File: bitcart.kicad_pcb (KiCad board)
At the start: 4 copper layers, 160 x 90 mm, 151 parts, among them J1 Conn_01x03, J10 690-019-298-412, J11 USB_OTG, J12 10018783-11200TLF, J13 690-008-221-904, J14 Conn_02x05_Odd_Even, J15 Conn_01x22_Female, J16 Conn_01x22_Female, J17 Molex 470531000, J19 Barrel_Jack, J2 Conn_02x07_Odd_Even, J20 AMP171826-4, J22 690-019-298-412, J3 Conn_01x03, J4 Conn_01x22_Female, J5 Conn_01x22_Female, J6 THD-02-R, J7 Micro_SD_Card_Det, J8 THD-20-R, J9 THD-02-R, Q1 DMP3013SFV-7, U1 TPD4EUSB30, U11 EMC2301-1-ACZL-TR, U12 RT9742SNGV, U13 FSUSB42MUX, U14 74LVC1G07SE-7, U15 AP64501SP-13, U16 AP64501SP-13, U18 RT9742GGJ5, U2 TPD4EUSB30, U3 MagJack-A70-112-331N126, U4 TPD4EUSB30, U5 74LVC1G07SE-7, U6 USB2514B-I/M2, U7 AP22653W6, U8 PCF85063AT/AAZ, U9 74LVC1G07SE-7, Y1 24MHz, Y2 X32K768S301

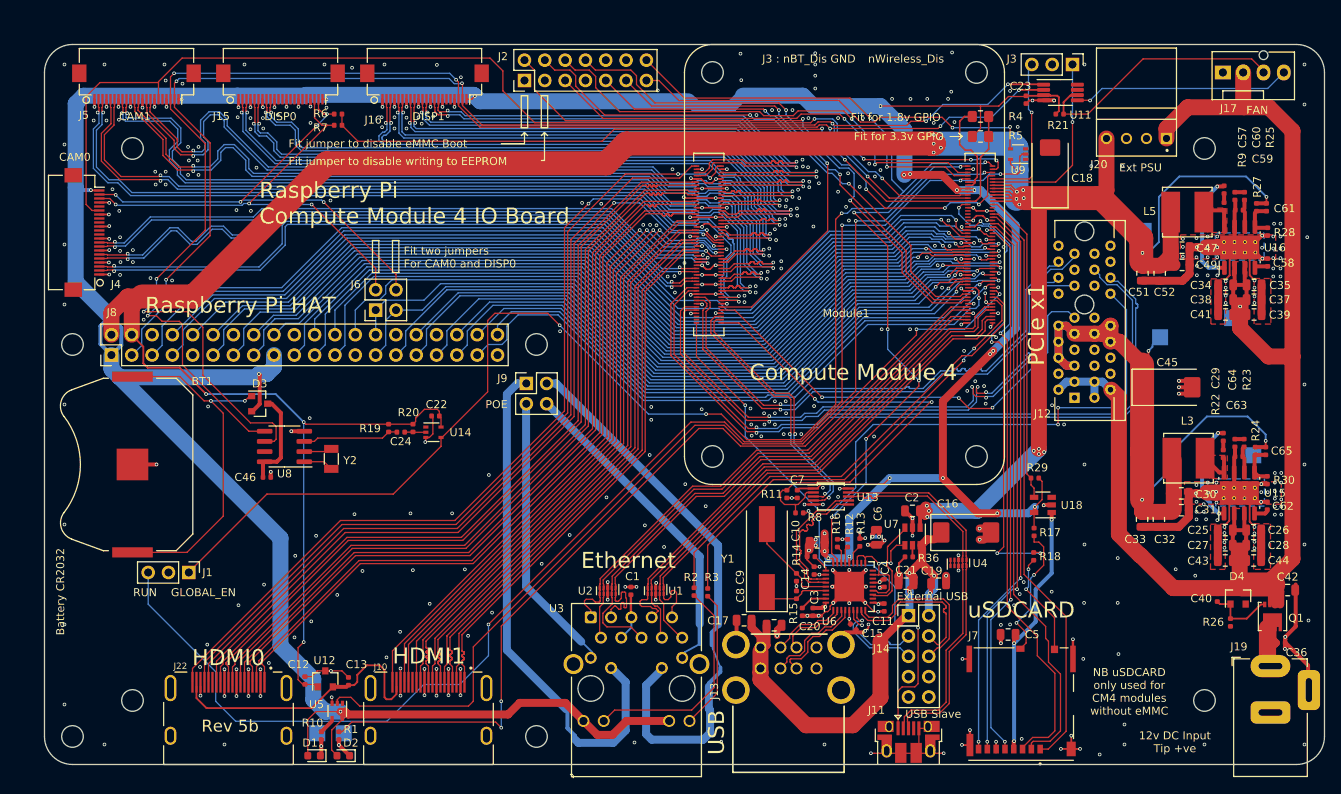
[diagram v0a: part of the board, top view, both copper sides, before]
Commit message: removed many unused parts
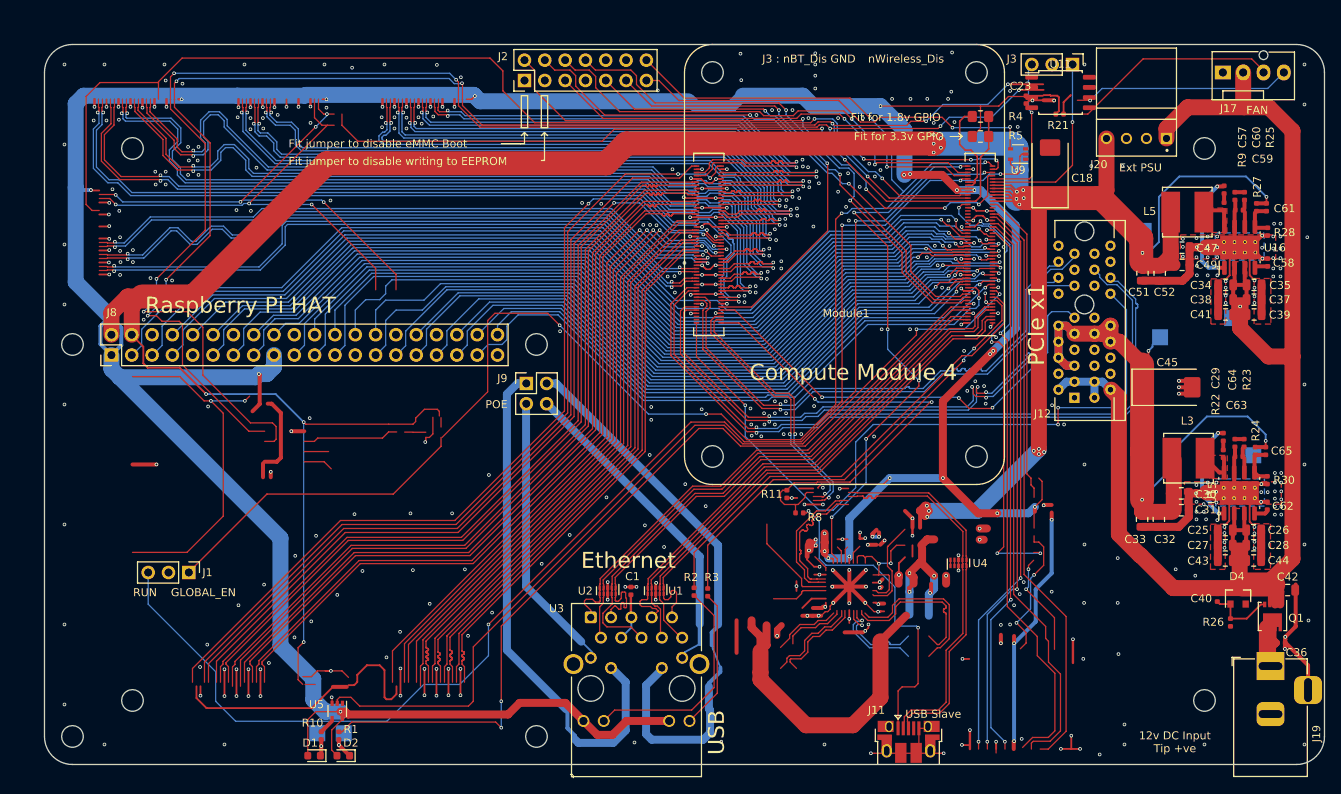
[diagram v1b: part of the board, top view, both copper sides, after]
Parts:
- removed BT1: Battery_Cell, Battery:BatteryHolder_Keystone_3034_1x20mm
- removed C10, C17, C19, C2, C20, C21, C5, C6: 10u, Capacitor_SMD:C_0805_2012Metric
- removed C11, C12, C13, C14, C15, C22, C24, C3, C4, C46, C7: 100n, Capacitor_SMD:C_0402_1005Metric
- removed C16: 100uF, Capacitor_Tantalum_SMD:CP_EIA-7343-31_Kemet-D
- removed C8, C9: 27pF, Capacitor_SMD:C_0402_1005Metric
- removed D3: BAT54C-7-F, Package_TO_SOT_SMD:SOT-23
- removed J10, J22: 690-019-298-412, CM4IO:EDAC 690-019-298-412
- removed J13: 690-008-221-904, CM4IO:MOLEX_USB_67298-4090
- removed J14: Conn_02x05_Odd_Even, Connector_PinHeader_2.54mm:PinHeader_2x05_P2.54mm_Vertical
- removed J15, J16, J4, J5: Conn_01x22_Female, CM4IO:Hirose_FH12-22S-0.5SH_1x22-1MP_P0.50mm_Horizontal
- removed J6: THD-02-R, Connector_PinHeader_2.54mm:PinHeader_2x02_P2.54mm_Vertical
- removed J7: Micro_SD_Card_Det, CM4IO:SDCARD_MOLEX_503398-1892
- removed R12, R13, R14, R16: 36K 1%, Resistor_SMD:R_0402_1005Metric
- removed R15, R29: 12K 1%, Resistor_SMD:R_0402_1005Metric
- removed R17, R18: nf, Resistor_SMD:R_0402_1005Metric
- removed R19, R20: 510K 1%, Resistor_SMD:R_0402_1005Metric
- removed R36: 15K 1%, Resistor_SMD:R_0402_1005Metric
- removed R6, R7: 2.2K 1%, Resistor_SMD:R_0402_1005Metric
- removed U12: RT9742SNGV, Package_TO_SOT_SMD:SOT-23
- removed U13: FSUSB42MUX, Package_SO:MSOP-10_3x3mm_P0.5mm
- removed U14: 74LVC1G07SE-7, Package_TO_SOT_SMD:SOT-353_SC-70-5
- removed U18: RT9742GGJ5, Package_TO_SOT_SMD:SOT-23-5
- removed U6: USB2514B-I/M2, Package_DFN_QFN:QFN-36-1EP_6x6mm_P0.5mm_EP3.7x3.7mm
- removed U7: AP22653W6, Package_TO_SOT_SMD:SOT-23-6
- removed U8: PCF85063AT/AAZ, Package_SO:SOIC-8_3.9x4.9mm_P1.27mm
- removed Y1: 24MHz, Crystal:Crystal_SMD_HC49-SD
- removed Y2: X32K768S301, Crystal:Crystal_SMD_3215-2Pin_3.2x1.5mm
- J19: footprint CM4IO:BarrelJack_Horizontal -> Connector_BarrelJack:BarrelJack_Horizontal
- U11: footprint Package_SO:MSOP-8_3x3mm_P0.65mm -> Package_SO:SOIC-8_5.23x5.23mm_P1.27mm
- U15: footprint CM4IO:SOIC-8-1EP_3.9x4.9mm_P1.27mm_EP2.95x4.9mm_Mask2.71x3.4mm_ThermalVias -> Package_SO:SOIC-8-1EP_3.9x4.9mm_P1.27mm_EP2.95x4.9mm_Mask2.71x3.4mm_ThermalVias
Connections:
- Module1 pad 115: /CM4_HighSpeed/CAM1_D0_N -> unconnected-(Module1-Pad115)
- Module1 pad 117: /CM4_HighSpeed/CAM1_D0_P -> unconnected-(Module1-Pad117)
- Module1 pad 121: /CM4_HighSpeed/CAM1_D1_N -> unconnected-(Module1-Pad121)
- Module1 pad 123: /CM4_HighSpeed/CAM1_D1_P -> unconnected-(Module1-Pad123)
- Module1 pad 127: /CM4_HighSpeed/CAM1_C_N -> unconnected-(Module1-Pad127)
- Module1 pad 128: /CM4_HighSpeed/CAM0_D0_N -> unconnected-(Module1-Pad128)
- Module1 pad 129: /CM4_HighSpeed/CAM1_C_P -> unconnected-(Module1-Pad129)
- Module1 pad 130: /CM4_HighSpeed/CAM0_D0_P -> unconnected-(Module1-Pad130)
- Module1 pad 133: /CM4_HighSpeed/CAM1_D2_N -> unconnected-(Module1-Pad133)
- Module1 pad 134: /CM4_HighSpeed/CAM0_D1_N -> unconnected-(Module1-Pad134)
- Module1 pad 135: /CM4_HighSpeed/CAM1_D2_P -> unconnected-(Module1-Pad135)
- Module1 pad 136: /CM4_HighSpeed/CAM0_D1_P -> unconnected-(Module1-Pad136)
- Module1 pad 139: /CM4_HighSpeed/CAM1_D3_N -> unconnected-(Module1-Pad139)
- Module1 pad 140: /CM4_HighSpeed/CAM0_C_N -> unconnected-(Module1-Pad140)
- Module1 pad 141: /CM4_HighSpeed/CAM1_D3_P -> unconnected-(Module1-Pad141)
- Module1 pad 142: /CM4_HighSpeed/CAM0_C_P -> unconnected-(Module1-Pad142)
- Module1 pad 143: /CM4_HighSpeed/HDMI1_HOTPLUG -> unconnected-(Module1-Pad143)
- Module1 pad 145: /CM4_HighSpeed/HDMI1_SDA -> unconnected-(Module1-Pad145)
- Module1 pad 146: /CM4_HighSpeed/HDMI1_D2_P -> unconnected-(Module1-Pad146)
- Module1 pad 147: /CM4_HighSpeed/HDMI1_SCL -> unconnected-(Module1-Pad147)
- Module1 pad 148: /CM4_HighSpeed/HDMI1_D2_N -> unconnected-(Module1-Pad148)
- Module1 pad 149: /CM4_HighSpeed/HDMI1_CEC -> unconnected-(Module1-Pad149)
- Module1 pad 151: /CM4_HighSpeed/HDMI0_CEC -> unconnected-(Module1-Pad151)
- Module1 pad 152: /CM4_HighSpeed/HDMI1_D1_P -> unconnected-(Module1-Pad152)
- Module1 pad 153: /CM4_HighSpeed/HDMI0_HOTPLUG -> unconnected-(Module1-Pad153)
- Module1 pad 154: /CM4_HighSpeed/HDMI1_D1_N -> unconnected-(Module1-Pad154)
- Module1 pad 157: /CM4_HighSpeed/DSI0_D0_N -> unconnected-(Module1-Pad157)
- Module1 pad 158: /CM4_HighSpeed/HDMI1_D0_P -> unconnected-(Module1-Pad158)
- Module1 pad 159: /CM4_HighSpeed/DSI0_D0_P -> unconnected-(Module1-Pad159)
- Module1 pad 160: /CM4_HighSpeed/HDMI1_D0_N -> unconnected-(Module1-Pad160)
- Module1 pad 163: /CM4_HighSpeed/DSI0_D1_N -> unconnected-(Module1-Pad163)
- Module1 pad 164: /CM4_HighSpeed/HDMI1_CK_P -> unconnected-(Module1-Pad164)
- Module1 pad 165: /CM4_HighSpeed/DSI0_D1_P -> unconnected-(Module1-Pad165)
- Module1 pad 166: /CM4_HighSpeed/HDMI1_CK_N -> unconnected-(Module1-Pad166)
- Module1 pad 169: /CM4_HighSpeed/DSI0_C_N -> unconnected-(Module1-Pad169)
- Module1 pad 170: /CM4_HighSpeed/HDMI0_D2_P -> unconnected-(Module1-Pad170)
- Module1 pad 171: /CM4_HighSpeed/DSI0_C_P -> unconnected-(Module1-Pad171)
- Module1 pad 172: /CM4_HighSpeed/HDMI0_D2_N -> unconnected-(Module1-Pad172)
- Module1 pad 175: /CM4_HighSpeed/DSI1_D0_N -> unconnected-(Module1-Pad175)
- Module1 pad 176: /CM4_HighSpeed/HDMI0_D1_P -> unconnected-(Module1-Pad176)
- Module1 pad 177: /CM4_HighSpeed/DSI1_D0_P -> unconnected-(Module1-Pad177)
- Module1 pad 178: /CM4_HighSpeed/HDMI0_D1_N -> unconnected-(Module1-Pad178)
- Module1 pad 181: /CM4_HighSpeed/DSI1_D1_N -> unconnected-(Module1-Pad181)
- Module1 pad 182: /CM4_HighSpeed/HDMI0_D0_P -> unconnected-(Module1-Pad182)
- Module1 pad 183: /CM4_HighSpeed/DSI1_D1_P -> unconnected-(Module1-Pad183)
- Module1 pad 184: /CM4_HighSpeed/HDMI0_D0_N -> unconnected-(Module1-Pad184)
- Module1 pad 187: /CM4_HighSpeed/DSI1_C_N -> unconnected-(Module1-Pad187)
- Module1 pad 188: /CM4_HighSpeed/HDMI0_CK_P -> unconnected-(Module1-Pad188)
- Module1 pad 189: /CM4_HighSpeed/DSI1_C_P -> unconnected-(Module1-Pad189)
- Module1 pad 190: /CM4_HighSpeed/HDMI0_CK_N -> unconnected-(Module1-Pad190)
- Module1 pad 193: /CM4_HighSpeed/DSI1_D2_N -> unconnected-(Module1-Pad193)
- Module1 pad 194: /CM4_HighSpeed/DSI1_D3_N -> unconnected-(Module1-Pad194)
- Module1 pad 195: /CM4_HighSpeed/DSI1_D2_P -> unconnected-(Module1-Pad195)
- Module1 pad 196: /CM4_HighSpeed/DSI1_D3_P -> unconnected-(Module1-Pad196)
- Module1 pad 199: /CM4_HighSpeed/HDMI0_SDA -> unconnected-(Module1-Pad199)
- Module1 pad 200: /CM4_HighSpeed/HDMI0_SCL -> unconnected-(Module1-Pad200)
- Module1 pad 61: /CM4_GPIO ( Ethernet, GPIO, SDCARD)/SD_DAT3 -> unconnected-(Module1-Pad61)
- Module1 pad 62: /CM4_GPIO ( Ethernet, GPIO, SDCARD)/SD_CMD -> unconnected-(Module1-Pad62)
- Module1 pad 63: /CM4_GPIO ( Ethernet, GPIO, SDCARD)/SD_DAT0 -> unconnected-(Module1-Pad63)
- Module1 pad 67: /CM4_GPIO ( Ethernet, GPIO, SDCARD)/SD_DAT1 -> unconnected-(Module1-Pad67)
- Module1 pad 69: /CM4_GPIO ( Ethernet, GPIO, SDCARD)/SD_DAT2 -> unconnected-(Module1-Pad69)
- Module1 pad 80: /CM4_HighSpeed/SCL0 -> /CM4_GPIO ( Ethernet, GPIO, SDCARD)/SCL0
- Module1 pad 82: /CM4_HighSpeed/SDA0 -> /CM4_GPIO ( Ethernet, GPIO, SDCARD)/SDA0
- Module1 pad 97: /CM4_HighSpeed/CAM_GPIO -> /CM4_GPIO ( Ethernet, GPIO, SDCARD)/CAM_GPIO
- U11 pad 1: /CM4_HighSpeed/SDA0 -> /RTC , Wakeup, FAN/SDA
- U11 pad 2: /CM4_HighSpeed/SCL0 -> /RTC , Wakeup, FAN/SCL
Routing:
- net (no net): track 0.00 -> 568.8 mm, vias 0 -> 25
- net /CM4_GPIO ( Ethernet, GPIO, SDCARD)/SCL0: track 0.00 -> 395.8 mm, vias 0 -> 16
- net /CM4_HighSpeed/SCL0: track 201.2 -> 0.00 mm, vias 8 -> 0
- net /CM4_HighSpeed/SDA0: track 194.6 -> 0.00 mm, vias 8 -> 0
- net /CM4_HighSpeed/CAM_GPIO: track 143.1 -> 0.00 mm, vias 4 -> 0
- net /CM4_GPIO ( Ethernet, GPIO, SDCARD)/CAM_GPIO: track 0.00 -> 143.1 mm, vias 0 -> 4
- net unconnected-(Module1-Pad153): track 0.00 -> 108.0 mm, vias 0 -> 2
- net /CM4_HighSpeed/HDMI0_HOTPLUG: track 108.0 -> 0.00 mm, vias 2 -> 0
- net unconnected-(Module1-Pad199): track 0.00 -> 106.8 mm, vias 0 -> 2
- net /CM4_HighSpeed/HDMI0_SDA: track 106.8 -> 0.00 mm, vias 2 -> 0
- net unconnected-(Module1-Pad115): track 0.00 -> 104.5 mm, vias 0 -> 2
- net /CM4_HighSpeed/CAM1_D0_N: track 104.5 -> 0.00 mm, vias 2 -> 0
- net unconnected-(Module1-Pad117): track 0.00 -> 104.5 mm, vias 0 -> 2
- net /CM4_HighSpeed/CAM1_D0_P: track 104.5 -> 0.00 mm, vias 2 -> 0
- net unconnected-(Module1-Pad133): track 0.00 -> 104.5 mm, vias 0 -> 2
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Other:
- board text removed: "Battery CR2032"
- board text removed: "CAM0"
- board text removed: "CAM1"
- board text removed: "DISP0"
- board text removed: "DISP1"
- board text removed: "External USB"
- board text removed: "Fit two jumpers For CAM0 and DISP0"
- board text removed: "HDMI0"
- board text removed: "HDMI1"
- board text removed: "NB uSDCARD only used for CM4 modules without eMMC"
- board text removed: "Raspberry Pi Compute Module 4 IO Board"
- board text removed: "Rev 5b"
- board text removed: "uSDCARD"

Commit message: removed unused components
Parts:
- removed C1, C29, C40, C57, C58, C62: 100n, Capacitor_SMD:C_0402_1005Metric
- removed C18, C45: 100uF, Capacitor_Tantalum_SMD:CP_EIA-7343-31_Kemet-D
- removed C25, C26, C27, C28, C34, C35, C37, C38, C39, C41, C42, C43, C44: 10u 35v, Capacitor_SMD:C_0805_2012Metric
- removed C30, C31, C32, C33, C47, C49, C51, C52: 10u, Capacitor_SMD:C_0805_2012Metric
- removed C36: 100n 100v, Capacitor_SMD:C_0402_1005Metric
- removed C59, C61, C63, C65: nf, Capacitor_SMD:C_0402_1005Metric
- removed C60, C64: 1.2nF, Capacitor_SMD:C_0402_1005Metric
- removed D4: MMBZ5242BLT3G, Diode_SMD:D_SOT-23_ANK
- removed H2, H3, H4, H5, H6, H7, H8: MountingHole, MountingHole:MountingHole_2.7mm_M2.5
- removed J12: 10018783-11200TLF, CM4IO:PCIex1-36
- removed J19: Barrel_Jack, Connector_BarrelJack:BarrelJack_Horizontal
- removed J20: AMP171826-4, 171826-4:TE_171826-4
- removed J9: THD-02-R, Connector_PinHeader_2.54mm:PinHeader_2x02_P2.54mm_Vertical
- removed L3, L5: SRN6045TA-3R3Y, Inductor_SMD:L_Bourns_SRN6045TA
- removed R2, R3: 470R, Resistor_SMD:R_0402_1005Metric
- removed R22, R9: 10R, Resistor_SMD:R_0402_1005Metric
- removed R23, R26: 12K 1%, Resistor_SMD:R_0402_1005Metric
- removed R24: 47K 1%, Resistor_SMD:R_0402_1005Metric
- removed R25: 20K 1%, Resistor_SMD:R_0402_1005Metric
- removed R30: 15K 1%, Resistor_SMD:R_0402_1005Metric
- removed R4: nf, Resistor_SMD:R_0805_2012Metric_Pad1.15x1.40mm_HandSolder
- removed R5: 0R, Resistor_SMD:R_0805_2012Metric_Pad1.15x1.40mm_HandSolder
- removed TP1, TP2, TP4, TP6: TestPoint, TestPoint:TestPoint_Pad_2.0x2.0mm
- removed U1: TPD4EUSB30, Package_SON:USON-10_2.5x1.0mm_P0.5mm
- removed U15, U16: AP64501SP-13, Package_SO:SOIC-8-1EP_3.9x4.9mm_P1.27mm_EP2.95x4.9mm_Mask2.71x3.4mm_ThermalVias
- removed U3: MagJack-A70-112-331N126, CM4IO:TRJG0926HENL
- added C16: 100n, Capacitor_SMD:C_0402_1005Metric, F.Cu at (284.7, 241.8)
- added U10: MagJack-A70-112-331N126, CM4IO:TRJG0926HENL, F.Cu at (272.0, 233.4)
- added U6: TL432DBZ, Package_TO_SOT_SMD:SOT-23, F.Cu at (267.4, 221.2)
- added U7: TPD4EUSB30, Package_SON:USON-10_2.5x1.0mm_P0.5mm, F.Cu at (271.6, 222.2)
- added U8: TPD4EUSB30, Package_SON:USON-10_2.5x1.0mm_P0.5mm, F.Cu at (262.7, 217.3)
- Q1: value DMP3013SFV-7 -> Si7450DP; footprint Package_SON:Diodes_PowerDI3333-8 -> Package_TO_SOT_SMD:SOT-23
- R27: value 12K 1% -> 470R
- R28: value 2.2K 1% -> 470R
- TP3, TP5: moved to F.Cu
- U2: value TPD4EUSB30 -> LTV-817S; footprint Package_SON:USON-10_2.5x1.0mm_P0.5mm -> Package_DIP:SMDIP-4_W9.53mm
- moved Module1 161.6 mm to (110.8, 211.1), turned to -90 degrees
- moved U5 154.7 mm to (262.6, 201.5), turned to 90 degrees
- moved U11 122.9 mm to (125.9, 169.3)
- moved R21 119.3 mm to (120.1, 161.6)
- moved J17 119.1 mm to (136.8, 152.2)
- moved J2 119.1 mm to (49.5, 153.2)
- moved U9 119.1 mm to (111.2, 162.4)
- moved C23 119.1 mm to (112.2, 155.6)
- moved J3 119.1 mm to (118.0, 151.2)
- moved J8 91.3 mm to (110.1, 197.3)
- moved Q1 85.3 mm to (262.9, 221.2), turned to 90 degrees
- moved TP3 69.6 mm to (185.8, 150.7)
- moved TP5 68.9 mm to (181.8, 150.7)
- moved R10 67.6 mm to (181.2, 153.7), turned to 0 degrees
- moved H1 66.2 mm to (38.5, 193.6)
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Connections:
- net /CM4_GPIO ( Ethernet, GPIO, SDCARD)/+1.8v renamed /CM4_GPIO /+1.8v
- net /CM4_GPIO ( Ethernet, GPIO, SDCARD)/AIN0 renamed /CM4_GPIO /AIN0
- net /CM4_GPIO ( Ethernet, GPIO, SDCARD)/AIN1 renamed /CM4_GPIO /AIN1
- net /CM4_GPIO ( Ethernet, GPIO, SDCARD)/BT_nDis renamed /CM4_GPIO /BT_nDis
- net /CM4_GPIO ( Ethernet, GPIO, SDCARD)/EEPROM_nWP renamed /CM4_GPIO /EEPROM_nWP
- net /CM4_GPIO ( Ethernet, GPIO, SDCARD)/GLOBAL_EN renamed /CM4_GPIO /GLOBAL_EN
- net /CM4_GPIO ( Ethernet, GPIO, SDCARD)/GPIO10 renamed /CM4_GPIO /GPIO10
- net /CM4_GPIO ( Ethernet, GPIO, SDCARD)/GPIO11 renamed /CM4_GPIO /GPIO11
- net /CM4_GPIO ( Ethernet, GPIO, SDCARD)/GPIO12 renamed /CM4_GPIO /GPIO12
- net /CM4_GPIO ( Ethernet, GPIO, SDCARD)/GPIO13 renamed /CM4_GPIO /GPIO13
- net /CM4_GPIO ( Ethernet, GPIO, SDCARD)/GPIO14 renamed /CM4_GPIO /GPIO14
- net /CM4_GPIO ( Ethernet, GPIO, SDCARD)/GPIO15 renamed /CM4_GPIO /GPIO15
- net /CM4_GPIO ( Ethernet, GPIO, SDCARD)/GPIO16 renamed /CM4_GPIO /GPIO16
- net /CM4_GPIO ( Ethernet, GPIO, SDCARD)/GPIO17 renamed /CM4_GPIO /GPIO17
- net /CM4_GPIO ( Ethernet, GPIO, SDCARD)/GPIO18 renamed /CM4_GPIO /GPIO18
- net /CM4_GPIO ( Ethernet, GPIO, SDCARD)/GPIO19 renamed /CM4_GPIO /GPIO19
- net /CM4_GPIO ( Ethernet, GPIO, SDCARD)/GPIO2 renamed /CM4_GPIO /GPIO2
- net /CM4_GPIO ( Ethernet, GPIO, SDCARD)/GPIO20 renamed /CM4_GPIO /GPIO20
- net /CM4_GPIO ( Ethernet, GPIO, SDCARD)/GPIO21 renamed /CM4_GPIO /GPIO21
- net /CM4_GPIO ( Ethernet, GPIO, SDCARD)/GPIO22 renamed /CM4_GPIO /GPIO22
- net /CM4_GPIO ( Ethernet, GPIO, SDCARD)/GPIO23 renamed /CM4_GPIO /GPIO23
- net /CM4_GPIO ( Ethernet, GPIO, SDCARD)/GPIO24 renamed /CM4_GPIO /GPIO24
- net /CM4_GPIO ( Ethernet, GPIO, SDCARD)/GPIO25 renamed /CM4_GPIO /GPIO25
- net /CM4_GPIO ( Ethernet, GPIO, SDCARD)/GPIO26 renamed /CM4_GPIO /GPIO26
- net /CM4_GPIO ( Ethernet, GPIO, SDCARD)/GPIO27 renamed /CM4_GPIO /GPIO27
- net /CM4_GPIO ( Ethernet, GPIO, SDCARD)/GPIO3 renamed /CM4_GPIO /GPIO3
- net /CM4_GPIO ( Ethernet, GPIO, SDCARD)/GPIO4 renamed /CM4_GPIO /GPIO4
- net /CM4_GPIO ( Ethernet, GPIO, SDCARD)/GPIO5 renamed /CM4_GPIO /GPIO5
- net /CM4_GPIO ( Ethernet, GPIO, SDCARD)/GPIO6 renamed /CM4_GPIO /GPIO6
- net /CM4_GPIO ( Ethernet, GPIO, SDCARD)/GPIO7 renamed /CM4_GPIO /GPIO7
- net /CM4_GPIO ( Ethernet, GPIO, SDCARD)/GPIO8 renamed /CM4_GPIO /GPIO8
- net /CM4_GPIO ( Ethernet, GPIO, SDCARD)/GPIO9 renamed /CM4_GPIO /GPIO9
- net /CM4_GPIO ( Ethernet, GPIO, SDCARD)/ID_SC renamed /CM4_GPIO /ID_SC
- net /CM4_GPIO ( Ethernet, GPIO, SDCARD)/ID_SD renamed /CM4_GPIO /ID_SD
- net /CM4_GPIO ( Ethernet, GPIO, SDCARD)/RUN_PG renamed /CM4_GPIO /RUN_PG
- net /CM4_GPIO ( Ethernet, GPIO, SDCARD)/Reserved renamed /CM4_GPIO /Reserved
- net /CM4_GPIO ( Ethernet, GPIO, SDCARD)/SCL0 renamed /CM4_GPIO /SCL0
- net /CM4_GPIO ( Ethernet, GPIO, SDCARD)/SDA0 renamed /CM4_GPIO /SDA0
- net /CM4_GPIO ( Ethernet, GPIO, SDCARD)/SD_PWR_ON renamed /CM4_GPIO /SD_PWR_ON
- net /CM4_GPIO ( Ethernet, GPIO, SDCARD)/SYNC_IN renamed /CM4_GPIO /SYNC_IN
- net /CM4_GPIO ( Ethernet, GPIO, SDCARD)/SYNC_OUT renamed /CM4_GPIO /SYNC_OUT
- net /CM4_GPIO ( Ethernet, GPIO, SDCARD)/WL_nDis renamed /CM4_GPIO /WL_nDis
- net /CM4_GPIO ( Ethernet, GPIO, SDCARD)/nPWR_LED renamed /CM4_GPIO /nPWR_LED
- net /CM4_GPIO ( Ethernet, GPIO, SDCARD)/nRPIBOOT renamed /CM4_GPIO /nRPIBOOT
- net /RTC , Wakeup, FAN/SCL renamed /FAN/SCL
- net /RTC , Wakeup, FAN/SDA renamed /FAN/SDA
- J17 pad 2: /+12v -> /FAN/+12v
- J2 pad 11: /CM4_GPIO ( Ethernet, GPIO, SDCARD)/TV_OUT -> unconnected-(J2-Pad11)
- Module1 pad 10: /CM4_GPIO ( Ethernet, GPIO, SDCARD)/TRD0_N -> /CM4_GPIO /TRD0_N
- Module1 pad 102: /CM4_HighSpeed/PCIE_CLK_nREQ -> unconnected-(Module1-Pad102)
- Module1 pad 11: /CM4_GPIO ( Ethernet, GPIO, SDCARD)/TRD2_P -> /CM4_GPIO /TRD2_P
- Module1 pad 111: /CM4_GPIO ( Ethernet, GPIO, SDCARD)/TV_OUT -> unconnected-(Module1-Pad111)
- Module1 pad 12: /CM4_GPIO ( Ethernet, GPIO, SDCARD)/TRD0_P -> /CM4_GPIO /TRD0_P
- Module1 pad 15: /CM4_GPIO ( Ethernet, GPIO, SDCARD)/ETH_LEDY -> /CM4_GPIO /ETH_LEDY
- Module1 pad 17: /CM4_GPIO ( Ethernet, GPIO, SDCARD)/ETH_LEDG -> /CM4_GPIO /ETH_LEDG
- Module1 pad 3: /CM4_GPIO ( Ethernet, GPIO, SDCARD)/TRD3_P -> /CM4_GPIO /TRD3_P
- Module1 pad 4: /CM4_GPIO ( Ethernet, GPIO, SDCARD)/TRD1_P -> /CM4_GPIO /TRD1_P
- Module1 pad 5: /CM4_GPIO ( Ethernet, GPIO, SDCARD)/TRD3_N -> /CM4_GPIO /TRD3_N
- Module1 pad 57: /CM4_GPIO ( Ethernet, GPIO, SDCARD)/SD_CLK -> unconnected-(Module1-Pad57)
- Module1 pad 6: /CM4_GPIO ( Ethernet, GPIO, SDCARD)/TRD1_N -> /CM4_GPIO /TRD1_N
- Module1 pad 78: /CM4_GPIO ( Ethernet, GPIO, SDCARD)/GPIO_VREF -> /+3.3v
- Module1 pad 9: /CM4_GPIO ( Ethernet, GPIO, SDCARD)/TRD2_N -> /CM4_GPIO /TRD2_N
- Module1 pad 97: /CM4_GPIO ( Ethernet, GPIO, SDCARD)/CAM_GPIO -> unconnected-(Module1-Pad97)
- Q1 pad 1: /+12v -> Net-(D5-Pad2)
- Q1 pad 2: /+12v -> Net-(Q1-Pad2)
- Q1 pad 3: /+12v -> /PoE/W1
- R27 pad 1: /+5v -> Net-(R27-Pad1)
- R27 pad 2: Net-(C61-Pad2) -> /PoE/ETH_LEDG
- R28 pad 1: Net-(C61-Pad2) -> Net-(R28-Pad1)
- R28 pad 2: GND -> /PoE/ETH_LEDY
- U2 pad 1: /CM4_GPIO ( Ethernet, GPIO, SDCARD)/TRD1_P -> /PoE/W3
- U2 pad 2: /CM4_GPIO ( Ethernet, GPIO, SDCARD)/TRD1_N -> /PoE/W4
- U2 pad 3: GND -> /PoE/GND1
- U2 pad 4: /CM4_GPIO ( Ethernet, GPIO, SDCARD)/TRD0_N -> /PoE/COMP
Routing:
- net GND: track 874.5 -> 0.00 mm, vias 485 -> 0
- net (no net): track 568.8 -> 0.00 mm, vias 25 -> 0
- net /+3.3v: track 464.8 -> 0.00 mm, vias 30 -> 0
- net /CM4_GPIO /SCL0: track 395.8 -> 0.00 mm, vias 16 -> 0
- net /+5v: track 366.9 -> 0.00 mm, vias 23 -> 0
- net /CM4_GPIO /GLOBAL_EN: track 196.2 -> 0.00 mm, vias 5 -> 0
- net /+12v: track 189.7 -> 0.00 mm, vias 1 -> 0
- net /CM4_GPIO /RUN_PG: track 170.6 -> 0.00 mm, vias 4 -> 0
- net /CM4_GPIO ( Ethernet, GPIO, SDCARD)/CAM_GPIO: track 143.1 -> 0.00 mm, vias 4 -> 0
- net /CM4_GPIO /nPWR_LED: track 128.9 -> 0.00 mm, vias 2 -> 0
- net /CM4_GPIO /GPIO2: track 122.9 -> 0.00 mm, vias 1 -> 0
- net /CM4_GPIO /GPIO3: track 119.8 -> 0.00 mm, vias 1 -> 0
- net /CM4_GPIO /GPIO14: track 117.8 -> 0.00 mm, vias 1 -> 0
- net Net-(Module1-Pad21): track 116.6 -> 0.00 mm, vias 4 -> 0
- net /CM4_GPIO /GPIO4: track 116.5 -> 0.00 mm, vias 1 -> 0
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- removed copper zone on F.Cu, net /+12v
- removed copper zone on B.Cu, net GND
- removed copper zone on F.Cu, net GND
- removed copper zone on F.Cu, net Net-(L3-Pad1)
- removed copper zone on F.Cu, net Net-(L5-Pad1)
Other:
- board size 160 x 90 mm -> 253.4 x 82.2 mm
- board text added: "Board thickness : 1.56mm Finished copper weight inners : 1oz Finished copper weight outers : 1oz Material type : FR4 50R trace width 0.13mm@ 3GHz 90R diff pair width 0.147 spacing 0.253mm @ 2.5GHz 100R diff pair width 0.127 spacing 0.253mm @ 2GHz"
- board text removed: "12v DC Input Tip +ve"
- board text removed: "Board thickness : 1.56mm Finished copper weight inners : 1oz Finished copper weight outers : 1oz Board finish : OSP Material type : FR4 Colour of solder resists : Green Colour of silk screens : White Only on the top side Board to : UL94-V0 TG >=130 50R trace width 0.13mm@ 3GHz 90R diff pair width 0.147 spacing 0.253mm @ 2.5GHz 100R diff pair width 0.127 spacing 0.253mm @ 2GHz"
- board text removed: "Compute Module 4"
- board text removed: "Ethernet"
- board text removed: "Ext PSU"
- board text removed: "Fit for 1.8v GPIO"
- board text removed: "Fit for 3.3v GPIO"
- board text removed: "Fit jumper to disable eMMC Boot"
- board text removed: "Fit jumper to disable writing to EEPROM"
- board text removed: "J3 : nBT_Dis GND"
- board text removed: "PCIe x1"
- board text removed: "POE"
- board text removed: "USB"
- board text removed: "USB Slave"
- board text removed: "nWireless_Dis"

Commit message: added the M.2 connector and MP8008 footprints
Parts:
- removed J8: THD-20-R, Connector_PinHeader_2.54mm:PinHeader_2x20_P2.54mm_Vertical
- removed TP3, TP5: TestPoint, TestPoint:TestPoint_Pad_2.0x2.0mm
- added H2: M2.5 x 2.5mm SMD threaded standoff, bitcart:9774025151R, B.Cu at (150.4, 229.7)
- added U1: MP8008, bitcart:QFN-28_EP_4x5_Pitch0.5mm, F.Cu at (164.4, 207.2)
- added U12: MDT320M01001, bitcart:MDT320M01001, B.Cu at (72.2, 229.7)
- moved U5 110.2 mm to (152.8, 209.8)
- moved C16 103.7 mm to (181.0, 238.8)
- moved Q1 103.7 mm to (159.3, 218.2)
- moved U10 103.7 mm to (168.3, 230.5)
- moved U8 103.7 mm to (159.1, 214.4)
- moved U6 103.7 mm to (163.7, 218.2)
- moved U7 103.7 mm to (168.0, 219.3)
- moved U2 84.2 mm to (172.0, 207.6)
- moved U11 43.8 mm to (141.5, 210.2)
- moved Module1 31.1 mm to (79.8, 213.2)
- moved H1 21.0 mm to (57.8, 201.8)
- moved J17 15.7 mm to (142.5, 166.8)
- moved J11 2.52 mm to (177.9, 142.5)
- moved R8 1.16 mm to (186.7, 143.2)
- moved D2 1.13 mm to (177.7, 148.8)
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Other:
- board size 253.4 x 82.2 mm -> 129.4 x 54.6 mm
- board text removed: "Raspberry Pi HAT"

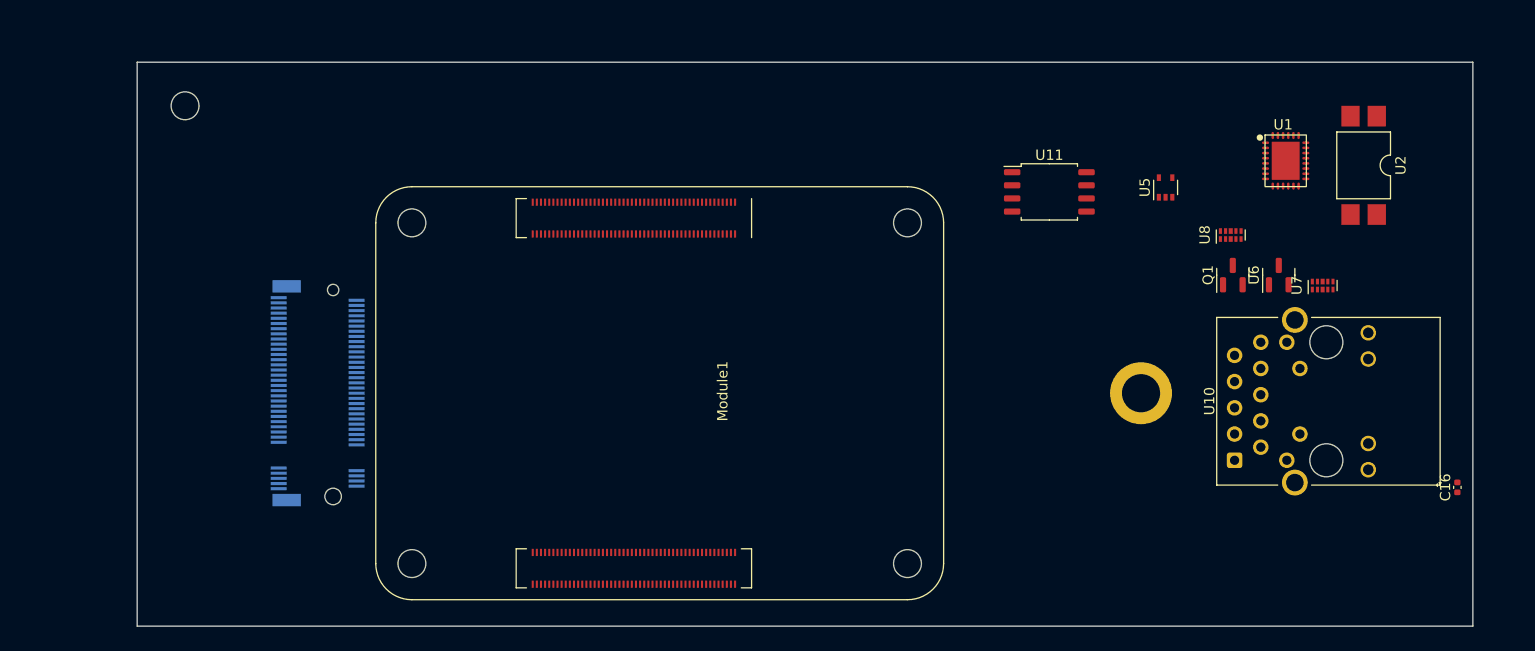
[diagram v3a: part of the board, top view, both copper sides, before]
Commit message: adding PoE parts
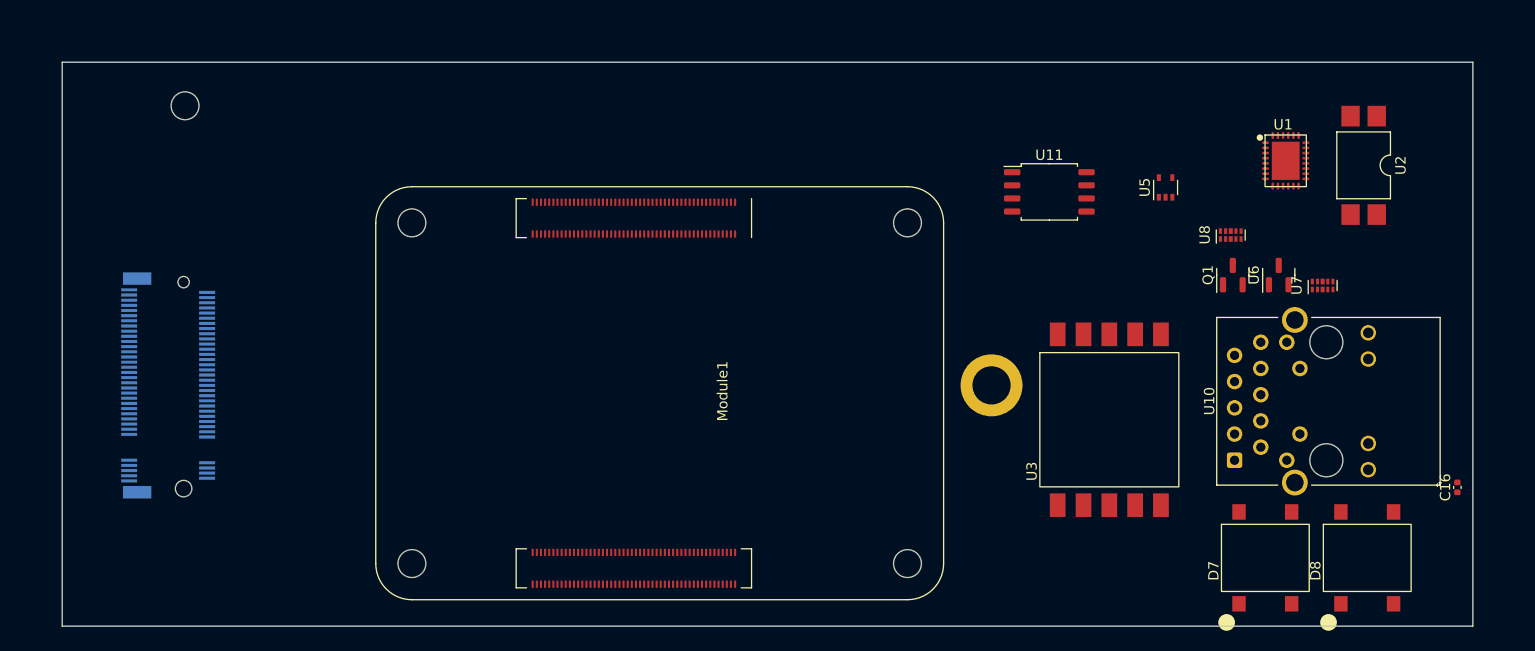
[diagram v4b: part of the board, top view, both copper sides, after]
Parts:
- added D7: DF01S, bitcart:DF01S, F.Cu at (162.4, 245.6)
- added D8: DF01S, bitcart:DF01S, F.Cu at (172.3, 245.6)
- added U3: 750310744, bitcart:750310744, F.Cu at (147.3, 232.3)
- moved H2 14.5 mm to (135.9, 228.9)
- moved U12 14.5 mm to (57.7, 228.9)
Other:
- board size 129.4 x 54.6 mm -> 136.6 x 54.6 mm
